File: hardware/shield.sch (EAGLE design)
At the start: 21 parts

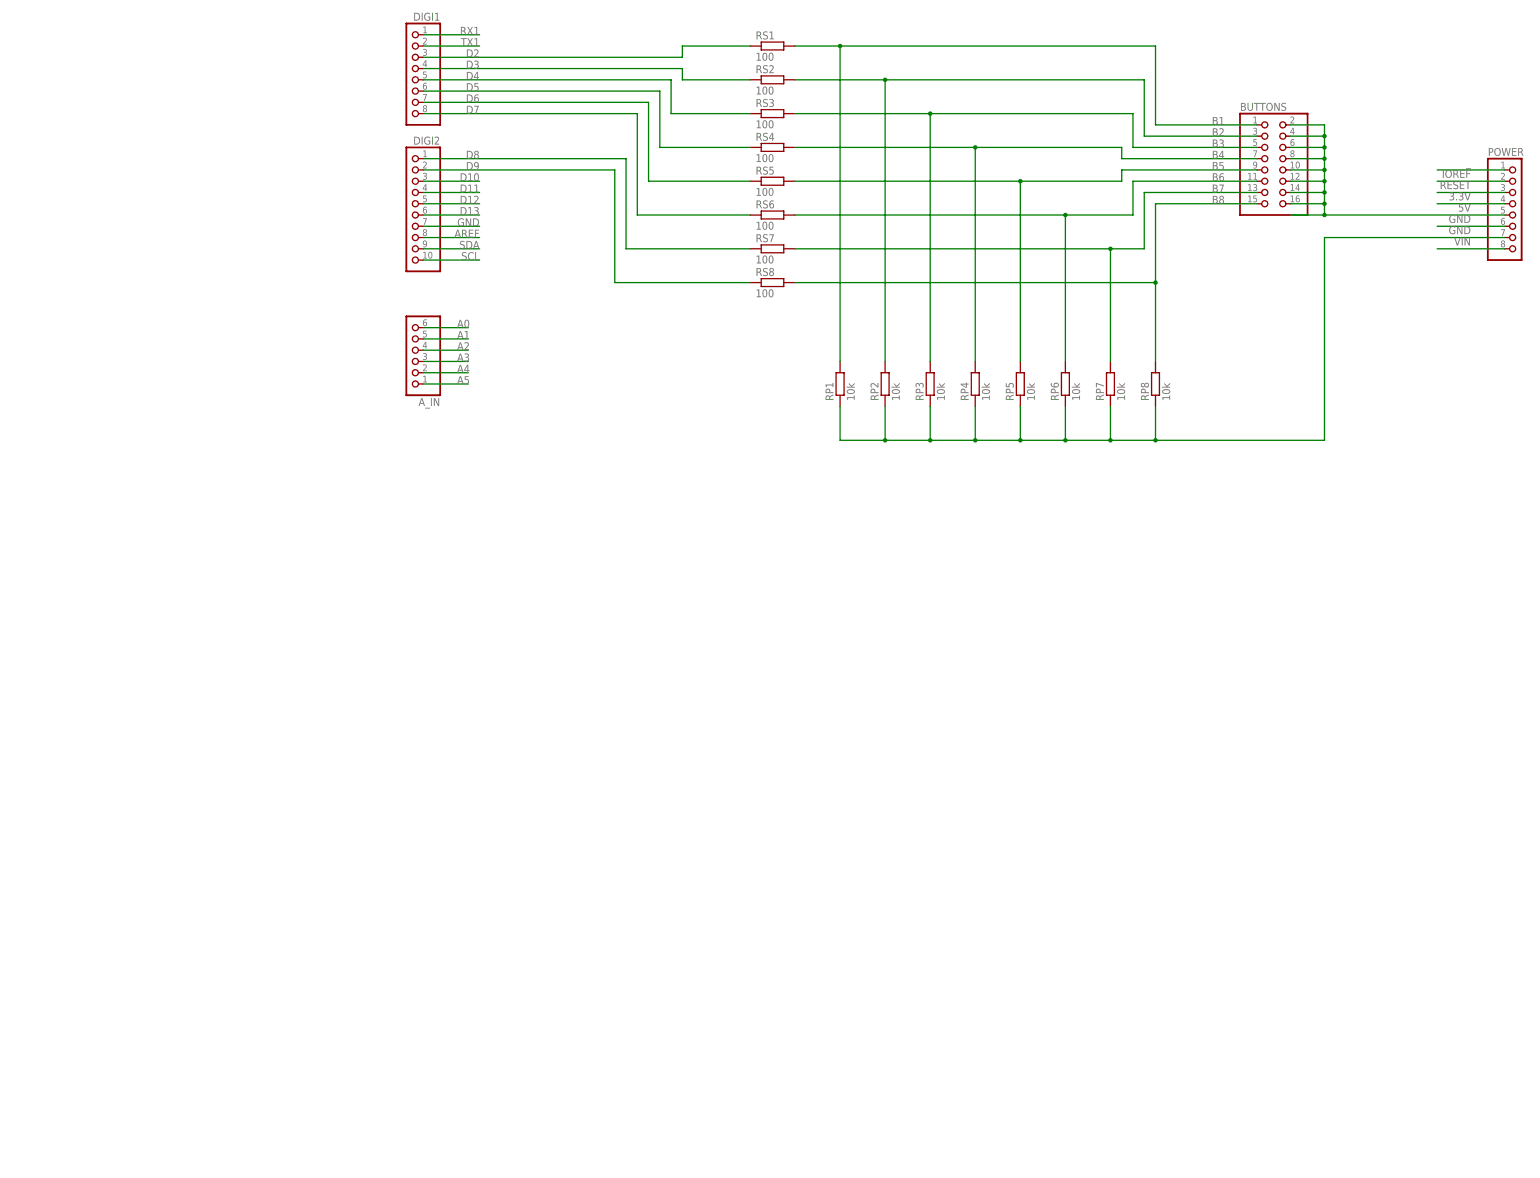
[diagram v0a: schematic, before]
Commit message: add poti connetions to schematic
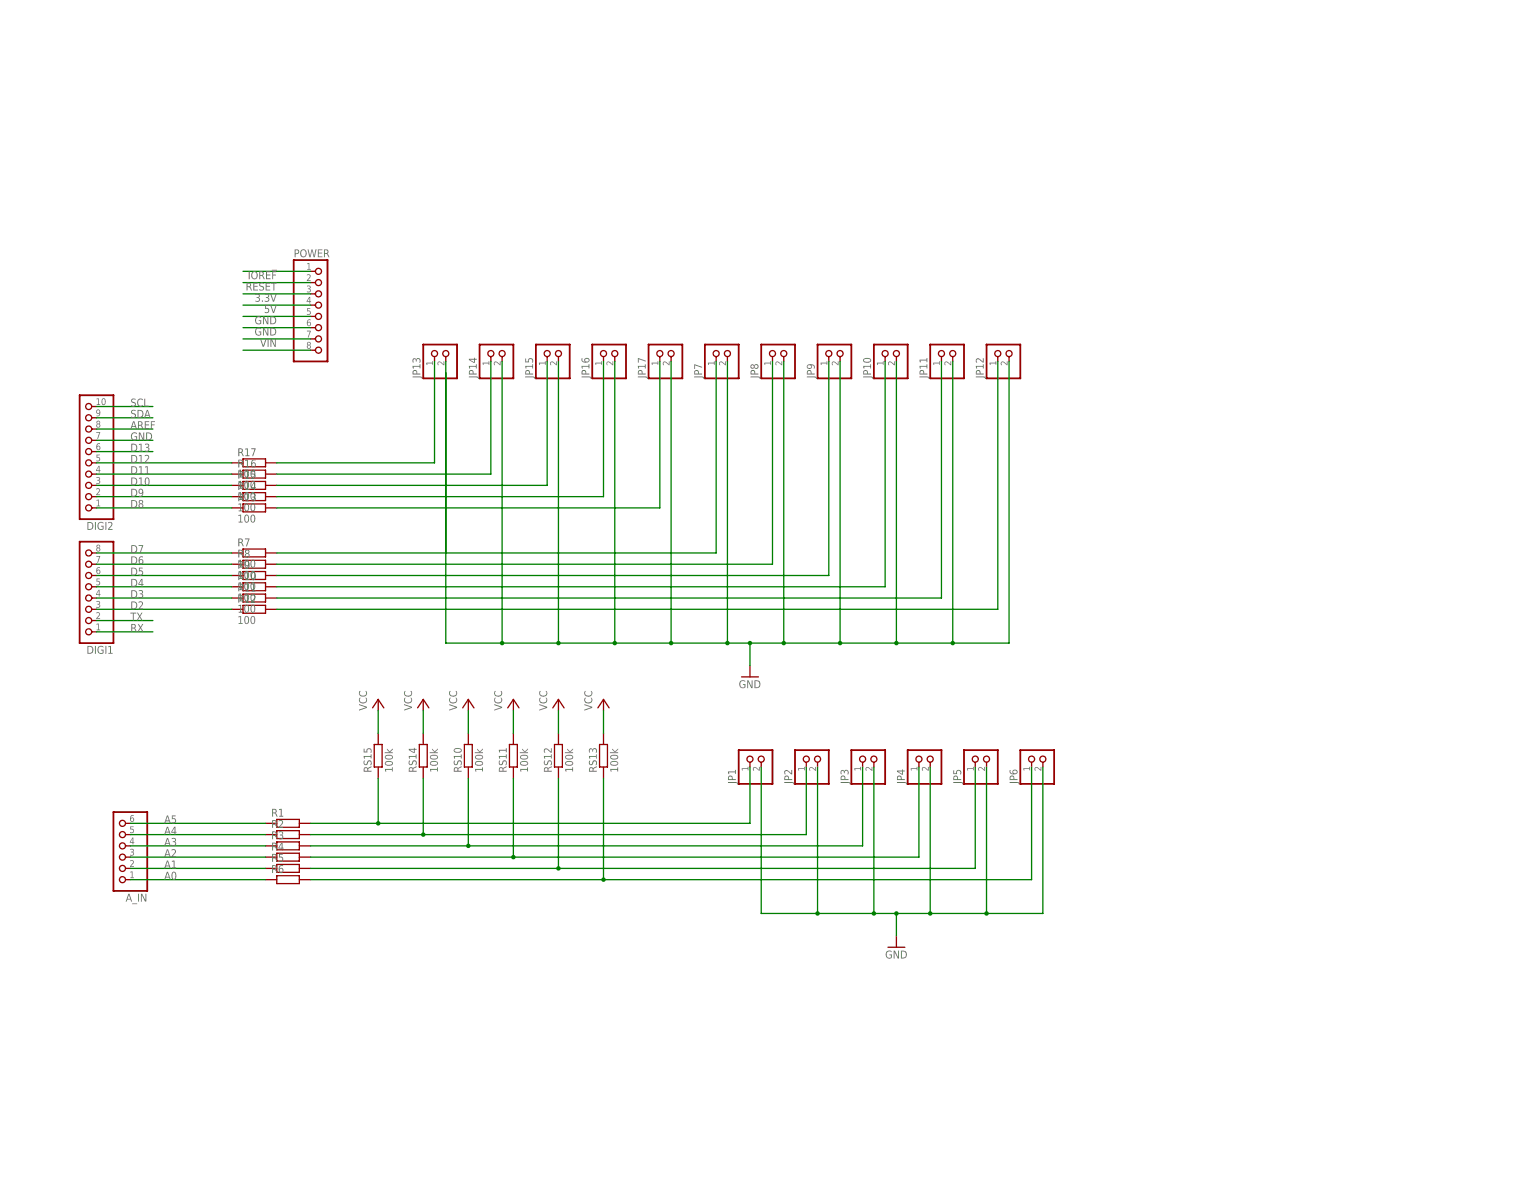
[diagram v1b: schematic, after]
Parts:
- removed BUTTONS: (no value), pinhead:PINHD-2X8
- removed RP1, RP2, RP3, RP6, RP7, RP8: 10k, rcl:R-EU_0207/7
- removed RP4, RP5: 10k, rcl:R-EU_0207/10
- removed RS1, RS2, RS3, RS4, RS5, RS6, RS7, RS8: 100, rcl:R-EU_0207/7
- added JP1, JP10, JP11, JP12, JP13, JP14, JP15, JP16, JP17, JP2, JP3, JP4, JP5, JP6, JP7, JP8, JP9: (no value), pinhead:PINHD-1X2
- added R1, R2, R3, R4, R5, R6: (no value), rcl:R-EU_0207/7
- added R10, R11, R12, R13, R14, R15, R16, R17, R7, R8, R9: 100, rcl:R-EU_0207/7
- added RS10, RS11, RS12, RS13, RS14, RS15: 100k, rcl:R-EU_0207/7
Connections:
- net RX1 renamed RX
- net TX1 renamed TX
- removed net B1: BUTTONS.1, RP1.2, RS1.2
- removed net B2: BUTTONS.3, RP2.2, RS2.2
- removed net B3: BUTTONS.5, RP3.2, RS3.2
- removed net B4: BUTTONS.7, RP4.2, RS4.2
- removed net B5: BUTTONS.9, RP5.2, RS5.2
- removed net B6: BUTTONS.11, RP6.2, RS6.2
- removed net B7: BUTTONS.13, RP7.2, RS7.2
- removed net B8: BUTTONS.15, RP8.2, RS8.2
- new net A10: JP17.1, R13.2
- new net A6: JP13.1, R17.2
- new net A7: JP14.1, R16.2
- new net A8: JP15.1, R15.2
- new net A9: JP16.1, R14.2
- new net N$1: JP13.2
- new net VCC: RS10.2, RS11.2, RS12.2, RS13.2, RS14.2, RS15.2
- net 5V: no longer BUTTONS.10, BUTTONS.12, BUTTONS.14, BUTTONS.16, BUTTONS.2, BUTTONS.4, BUTTONS.6, BUTTONS.8
- net A0: now also A_IN.1, JP1.1, JP7.1, R1.2, R6.1, R7.2, RS15.1; no longer A_IN.6
- net A1: now also A_IN.2, JP2.1, JP8.1, R2.2, R5.1, R8.2, RS14.1; no longer A_IN.5
- net A2: now also A_IN.3, JP3.1, JP9.1, R3.2, R4.1, R9.2, RS10.1; no longer A_IN.4
- net A3: now also A_IN.4, JP10.1, JP4.1, R10.2, R3.1, R4.2, RS11.1; no longer A_IN.3
- net A4: now also A_IN.5, JP11.1, JP5.1, R11.2, R2.1, R5.2, RS12.1; no longer A_IN.2
- net A5: now also A_IN.6, JP12.1, JP6.1, R1.1, R12.2, R6.2, RS13.1; no longer A_IN.1
- net D10: now also R15.1
- net D11: now also R16.1
- net D12: now also R17.1
- net D2: now also R12.1; no longer RS1.1
- net D3: now also R11.1; no longer RS2.1
- net D4: now also R10.1; no longer RS3.1
- net D5: now also R9.1; no longer RS4.1
- net D6: now also R8.1; no longer RS5.1
- net D7: now also R7.1; no longer RS6.1
- net D8: now also R13.1; no longer RS7.1
- net D9: now also R14.1; no longer RS8.1
- net GND: now also JP1.2, JP10.2, JP11.2, JP12.2, JP14.2, JP15.2, JP16.2, JP17.2, JP2.2, JP3.2, JP4.2, JP5.2, JP6.2, JP7.2, JP8.2, JP9.2; no longer RP1.1, RP2.1, RP3.1, RP4.1, RP5.1, RP6.1, RP7.1, RP8.1
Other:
- moved on the sheet: A_IN, DIGI1, DIGI2, POWER

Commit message: add poti driving circuit to schematic and layout.
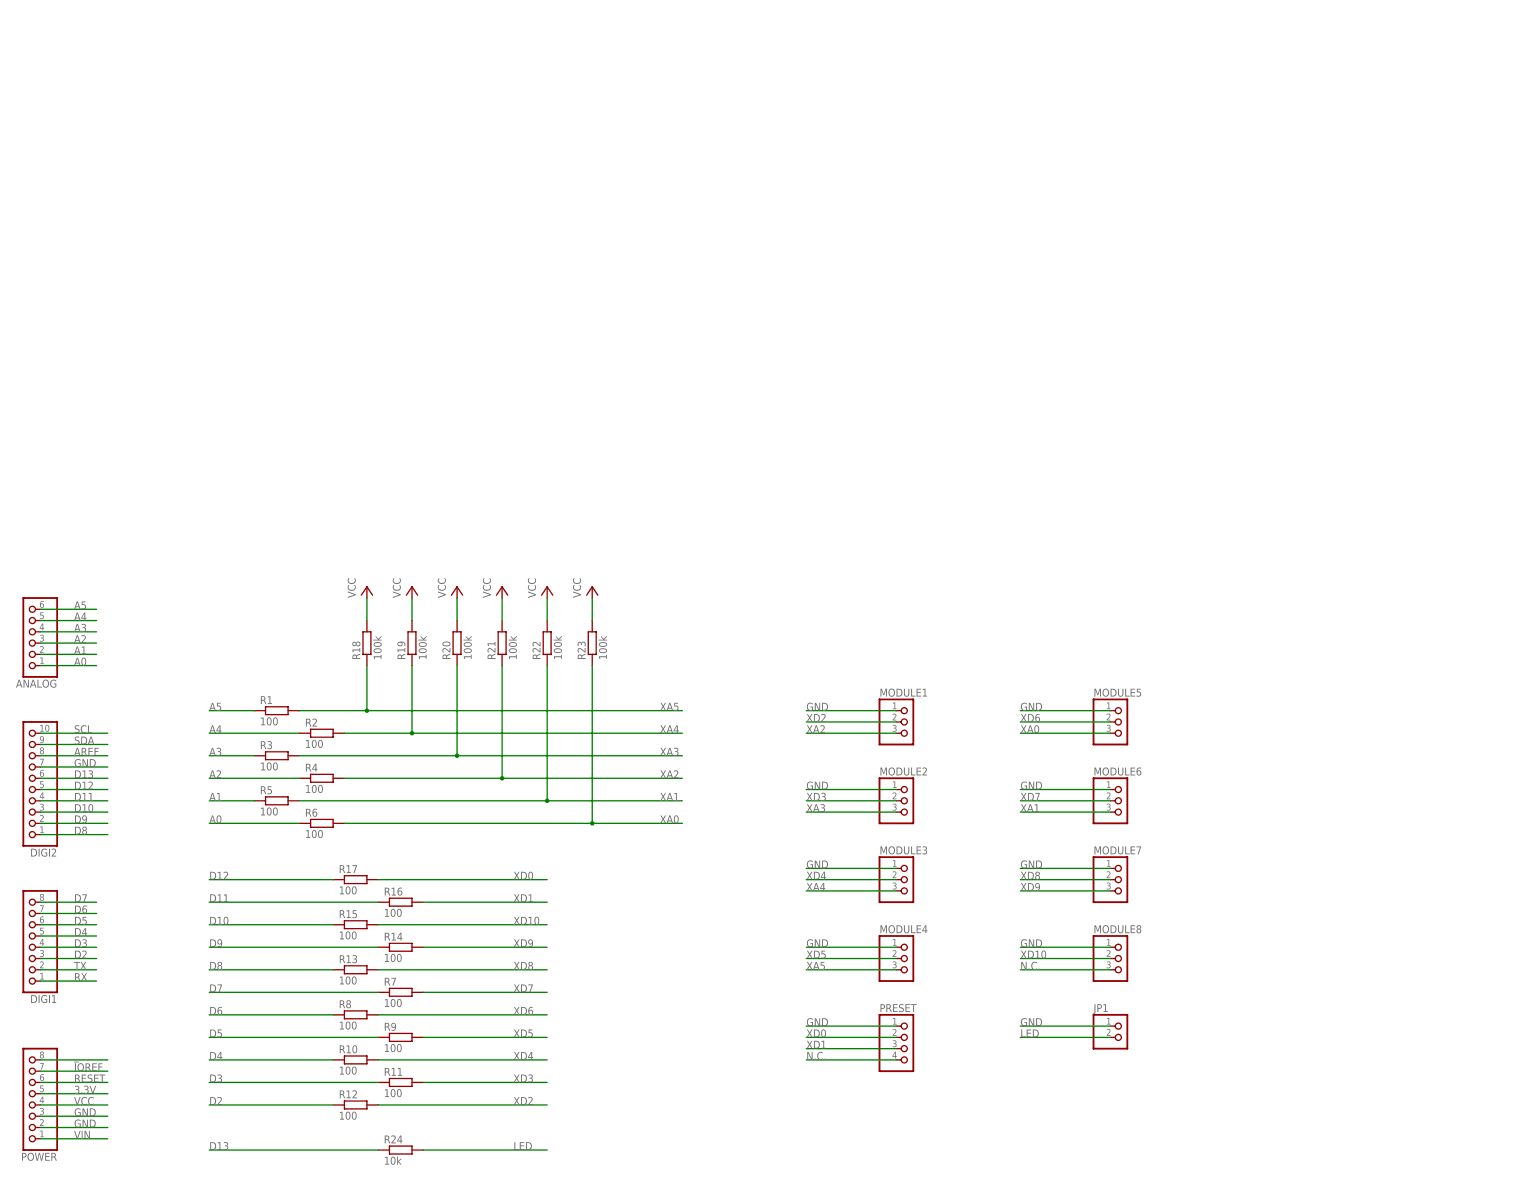
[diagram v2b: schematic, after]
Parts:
- removed A_IN: (no value), pinhead:PINHD-1X6
- removed JP10, JP11, JP12, JP13, JP14, JP15, JP16, JP17, JP2, JP3, JP4, JP5, JP6, JP7, JP8, JP9: (no value), pinhead:PINHD-1X2
- removed RS10, RS11, RS12, RS13, RS14, RS15: 100k, rcl:R-EU_0207/7
- added ANALOG: (no value), pinhead:PINHD-1X6
- added MODULE1, MODULE2, MODULE3, MODULE4, MODULE5, MODULE6, MODULE7, MODULE8: (no value), pinhead:PINHD-1X3
- added PRESET: (no value), pinhead:PINHD-1X4
- added R18, R19, R20, R21, R22, R23: 100k, rcl:R-EU_0207/7
- added R24: 10k, rcl:R-EU_0207/7
- R1, R2, R3, R4, R5, R6: value (none) -> 100
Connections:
- removed net 5V: POWER.5
- removed net A10: JP17.1, R13.2
- removed net A6: JP13.1, R17.2
- removed net A7: JP14.1, R16.2
- removed net A8: JP15.1, R15.2
- removed net A9: JP16.1, R14.2
- removed net N$1: JP13.2
- new net LED: JP1.2, R24.2
- new net N.C.: MODULE8.3, PRESET.4
- new net XA0: MODULE5.3, R23.1, R6.2
- new net XA1: MODULE6.3, R22.1, R5.2
- new net XA2: MODULE1.3, R21.1, R4.2
- new net XA3: MODULE2.3, R20.1, R3.2
- new net XA4: MODULE3.3, R19.1, R2.2
- new net XA5: MODULE4.3, R1.2, R18.1
- new net XD0: PRESET.2, R17.2
- new net XD1: PRESET.3, R16.2
- new net XD10: MODULE8.2, R15.2
- new net XD2: MODULE1.2, R12.2
- new net XD3: MODULE2.2, R11.2
- new net XD4: MODULE3.2, R10.2
- new net XD5: MODULE4.2, R9.2
- new net XD6: MODULE5.2, R8.2
- new net XD7: MODULE6.2, R7.2
- new net XD8: MODULE7.2, R13.2
- new net XD9: MODULE7.3, R14.2
- net 3.3V: now also POWER.5; no longer POWER.4
- net A0: now also ANALOG.1; no longer A_IN.1, JP1.1, JP7.1, R1.2, R7.2, RS15.1
- net A1: now also ANALOG.2; no longer A_IN.2, JP2.1, JP8.1, R2.2, R8.2, RS14.1
- net A2: now also ANALOG.3; no longer A_IN.3, JP3.1, JP9.1, R3.2, R9.2, RS10.1
- net A3: now also ANALOG.4; no longer A_IN.4, JP10.1, JP4.1, R10.2, R4.2, RS11.1
- net A4: now also ANALOG.5; no longer A_IN.5, JP11.1, JP5.1, R11.2, R5.2, RS12.1
- net A5: now also ANALOG.6; no longer A_IN.6, JP12.1, JP6.1, R12.2, R6.2, RS13.1
- net D13: now also R24.1
- net GND: now also JP1.1, MODULE1.1, MODULE2.1, MODULE3.1, MODULE4.1, MODULE5.1, MODULE6.1, MODULE7.1, MODULE8.1, POWER.2, POWER.3, PRESET.1; no longer JP1.2, JP10.2, JP11.2, JP12.2, JP14.2, JP15.2, JP16.2, JP17.2, JP2.2, JP3.2, JP4.2, JP5.2, JP6.2, JP7.2, JP8.2, JP9.2, POWER.6, POWER.7
- net IOREF: now also POWER.7; no longer POWER.2
- net RESET: now also POWER.6; no longer POWER.3
- net VCC: now also POWER.4, R18.2, R19.2, R20.2, R21.2, R22.2, R23.2; no longer RS10.2, RS11.2, RS12.2, RS13.2, RS14.2, RS15.2
- net VIN: now also POWER.1; no longer POWER.8
- net _: now also POWER.8; no longer POWER.1
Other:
- moved on the sheet: DIGI1, DIGI2, JP1, POWER, R1, R10, R11, R12, R13, R14, R15, R16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
